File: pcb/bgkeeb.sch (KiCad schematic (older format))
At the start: 102 parts, among them J1 Pimoroni, SW1 SW_Push, SW11 SW_Push, SW12 SW_Push, SW13 SW_Push, SW14 SW_Push, SW15 SW_Push, SW2 SW_Push, SW21 SW_Push, SW22 SW_Push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

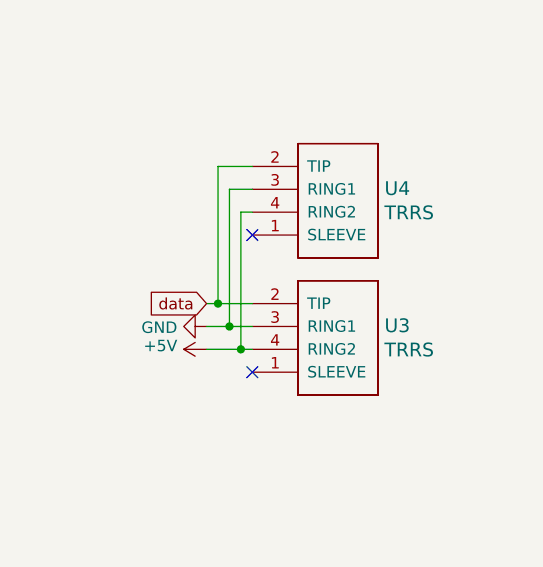
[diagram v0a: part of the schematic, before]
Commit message: updated TRRS order
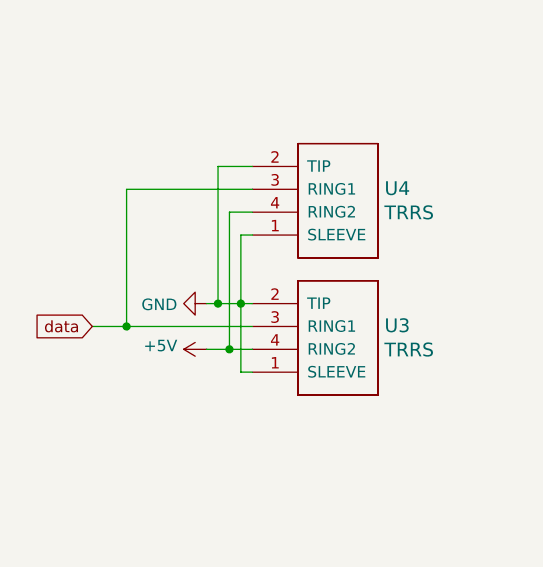
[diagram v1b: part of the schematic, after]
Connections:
- net GND: now also U3.1 (SLEEVE), U3.2 (TIP), U4.1 (SLEEVE), U4.2 (TIP); no longer U3.3 (RING1), U4.3 (RING1)
- net data: now also U3.3 (RING1), U4.3 (RING1); no longer U3.2 (TIP), U4.2 (TIP)
- no-connect marks 5 -> 3
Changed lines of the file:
@@
 Wire Wire Line
 	7450 4900 8100 4900
-$Comp
-L keebio:TRRS U3
-U 1 1 619B086F
-P 2650 8750
-F 0 "U3" H 2878 9053 60  0000 L CNN
-F 1 "TRRS" H 2878 8947 60  0000 L CNN
-F 2 "Keebio-Parts:TRRS-PJ-320A" H 2800 8750 60  0001 C CNN
-F 3 "" H 2800 8750 60  0001 C CNN
-	1    2650 8750
-	1    0    0    -1
-$EndComp
-Text GLabel 2100 8350 0    50   Input ~ 0
+Text GLabel 1600 8450 0    50   Input ~ 0
 data
 $Comp
 L power:GND #PWR0109
 U 1 1 619B75FE
-P 2100 8450
-F 0 "#PWR0109" H 2100 8200 50  0001 C CNN
-F 1 "GND" V 2105 8322 50  0000 R CNN
-F 2 "" H 2100 8450 50  0001 C CNN
-F 3 "" H 2100 8450 50  0001 C CNN
-	1    2100 8450
+P 2100 8350
+F 0 "#PWR0109" H 2100 8100 50  0001 C CNN
+F 1 "GND" V 2105 8222 50  0000 R CNN
+F 2 "" H 2100 8350 50  0001 C CNN
+F 3 "" H 2100 8350 50  0001 C CNN
+	1    2100 8350
 	0    1    1    0
 $EndComp
@@
 $EndComp
 Wire Wire Line
-	2100 8550 2250 8550
-Wire Wire Line
-	2100 8450 2200 8450
-Wire Wire Line
-	2100 8350 2150 8350
-Wire Wire Line
-	2300 7950 2250 7950
-Wire Wire Line
-	2250 7950 2250 8550
-Connection ~ 2250 8550
-Wire Wire Line
-	2250 8550 2300 8550
-Wire Wire Line
-	2300 7850 2200 7850
-Wire Wire Line
-	2200 7850 2200 8450
-Connection ~ 2200 8450
-Wire Wire Line
-	2200 8450 2300 8450
-Wire Wire Line
 	2300 7750 2150 7750
-Wire Wire Line
-	2150 7750 2150 8350
-Connection ~ 2150 8350
-Wire Wire Line
-	2150 8350 2300 8350
 Text GLabel 3150 3050 2    50   Input ~ 0
 data
@@
 	1    0    0    -1
 $EndComp
-NoConn ~ 2300 8050
-NoConn ~ 2300 8650
 Wire Wire Line
 	11750 7700 11900 7700
@@
 Wire Wire Line
 	3700 10500 3850 10500
+Wire Wire Line
+	2100 8550 2200 8550
+Wire Wire Line
+	2100 8350 2150 8350
+$Comp
+L keebio:TRRS U3
+U 1 1 619B086F
+P 2650 8750
+F 0 "U3" H 2878 9053 60  0000 L CNN
+F 1 "TRRS" H 2878 8947 60  0000 L CNN
+F 2 "Keebio-Parts:TRRS-PJ-320A" H 2800 8750 60  0001 C CNN
+F 3 "" H 2800 8750 60  0001 C CNN
+	1    2650 8750
+	1    0    0    -1
+$EndComp
+Wire Wire Line
+	2300 8650 2250 8650
+Wire Wire Line
+	2250 8650 2250 8350
+Connection ~ 2250 8350
+Wire Wire Line
+	2250 8350 2300 8350
+Wire Wire Line
+	2300 8050 2250 8050
+Wire Wire Line
+	2250 8050 2250 8350
+Wire Wire Line
+	2150 7750 2150 8350
+Connection ~ 2150 8350
+Wire Wire Line
+	2150 8350 2250 8350
+Wire Wire Line
+	2200 7950 2300 7950
+Connection ~ 2200 8550
+Wire Wire Line
+	2200 8550 2300 8550
+Wire Wire Line
+	2200 7950 2200 8550
+Wire Wire Line
+	1750 7850 1750 8450
+Wire Wire Line
+	1750 7850 2300 7850
+Wire Wire Line
+	1750 8450 2300 8450
+Wire Wire Line
+	1750 8450 1600 8450
+Connection ~ 1750 8450
 $EndSCHEMATC

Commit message: fixed a lot of things
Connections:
- net col0: now also U1.20 (A3/PF4); no longer U1.2 (RX1/PD2)
- net data: now also U1.2 (RX1/PD2); no longer U1.20 (A3/PF4)
- net row0: now also U1.18 (A1/PF6); no longer U1.24 (RAW)
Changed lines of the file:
@@
 Text GLabel 1750 3550 0    50   Input ~ 0
 row3
-Text GLabel 3150 2650 2    50   Input ~ 0
+Text GLabel 3150 3250 2    50   Input ~ 0
 row0
 Text GLabel 1750 3450 0    50   Input ~ 0
@@
 	0    -1   -1   0
 $EndComp
-Text GLabel 1750 2750 0    50   Input ~ 0
+Text GLabel 3150 3050 2    50   Input ~ 0
 col0
 Text GLabel 1750 3250 0    50   Input ~ 0
@@
 Wire Wire Line
 	2300 7750 2150 7750
-Text GLabel 3150 3050 2    50   Input ~ 0
+Text GLabel 1750 2750 0    50   Input ~ 0
 data
 Wire Wire Line
